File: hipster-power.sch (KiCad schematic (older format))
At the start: 14 parts, among them Q201 FDN340P, SW201 ON|OFF, U201 MCP73831, U202 NCP5501

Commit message: Rename power switch SK12D07VG5 -> SK12D07VG3
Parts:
- SW201: footprint libs:SK12D07VG5 -> libs:SK12D07VG3
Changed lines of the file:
@@
 F 0 "SW201" H 2850 4450 50  0000 C CNN
 F 1 "ON|OFF" H 2850 4250 50  0000 C CNN
-F 2 "libs:SK12D07VG5" H 2850 4350 50  0001 C CNN
+F 2 "libs:SK12D07VG3" H 2850 4350 50  0001 C CNN
 F 3 "" H 2850 4350 50  0000 C CNN
 F 4 "http://www.szlcsc.com/product/details_39247.html" H 7350 2250 60  0001 C CNN "LCSC"

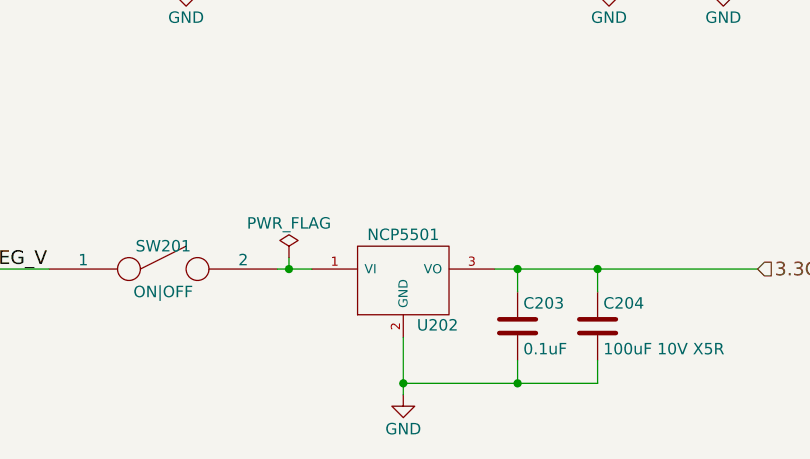
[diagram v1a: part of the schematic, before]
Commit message: Change 3.3V reg to XC6210, enlarge board to move power switch
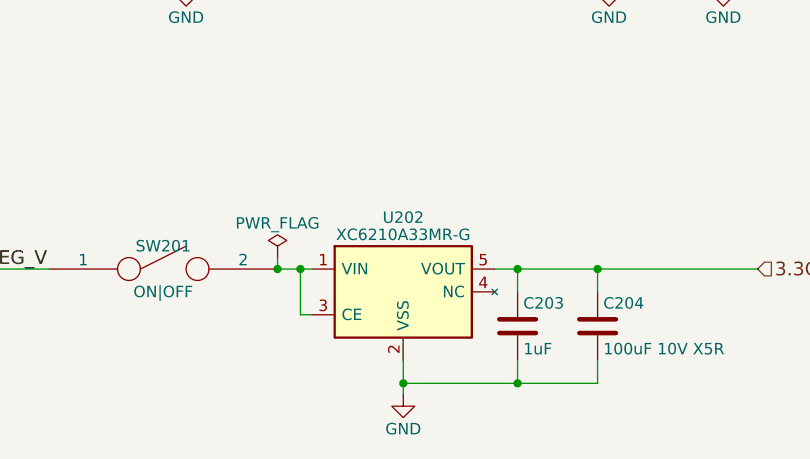
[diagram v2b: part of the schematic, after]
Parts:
- removed U202: NCP5501, libs:DPAK3.NCP5501, symbol NCP5501
- added U202: XC6210A33MR-G, symbol XC6210xxxxMR-G
- C203: value 0.1uF -> 1uF
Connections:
- net 3.3OUT: now also U202.5 (VOUT)
- net at SW201.2: now also U202.1 (VIN), U202.3 (CE)
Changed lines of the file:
@@
 LIBS:valves
 LIBS:ESP32-footprints-Shem-Lib
-LIBS:cp2102
-LIBS:NCP5501
-LIBS:mcp73831
-LIBS:q_pmos_gds
+LIBS:minimum-viable-badge-parts
 LIBS:minimum-viable-badge-cache
 EELAYER 25 0
@@
 UNREG_V
 $Comp
-L NCP5501 U202
-U 1 1 59286CBF
-P 3900 4400
-F 0 "U202" H 4050 4204 50  0000 C CNN
-F 1 "NCP5501" H 3900 4600 50  0000 C CNN
-F 2 "libs:DPAK3.NCP5501" H 3900 4400 50  0001 C CNN
-F 3 "" H 3900 4400 50  0000 C CNN
-F 4 "NCP5501DT33RKGOSCT-ND" H 3900 4400 60  0001 C CNN "Digikey PN"
-F 5 "http://www.digikey.com.au/product-detail/en/on-semiconductor/NCP5501DT33RKG/NCP5501DT33RKGOSCT-ND/3462404" H 3900 4400 60  0001 C CNN "Link"
-F 6 "NCP5501DT33RKG" H 3900 4400 60  0001 C CNN "Manufacture PN"
-F 7 "0.67" H 3900 4400 60  0001 C CNN "Unit Cost"
-	1    3900 4400
-	1    0    0    -1
-$EndComp
-$Comp
 L C C203
 U 1 1 59287000
 P 4400 4600
 F 0 "C203" H 4425 4700 50  0000 L CNN
-F 1 "0.1uF" H 4425 4500 50  0000 L CNN
+F 1 "1uF" H 4425 4500 50  0000 L CNN
 F 2 "Capacitors_SMD:C_0603_HandSoldering" H 4438 4450 50  0001 C CNN
 F 3 "" H 4400 4600 50  0000 C CNN
@@
 L PWR_FLAG #FLG025
 U 1 1 59A7D662
-P 3400 4300
-F 0 "#FLG025" H 3400 4375 50  0001 C CNN
-F 1 "PWR_FLAG" H 3400 4450 50  0000 C CNN
-F 2 "" H 3400 4300 50  0001 C CNN
-F 3 "" H 3400 4300 50  0001 C CNN
-	1    3400 4300
-	1    0    0    -1
-$EndComp
-Wire Wire Line
-	3400 4300 3400 4350
-Connection ~ 3400 4350
+P 3350 4300
+F 0 "#FLG025" H 3350 4375 50  0001 C CNN
+F 1 "PWR_FLAG" H 3350 4450 50  0000 C CNN
+F 2 "" H 3350 4300 50  0001 C CNN
+F 3 "" H 3350 4300 50  0001 C CNN
+	1    3350 4300
+	1    0    0    -1
+$EndComp
+Wire Wire Line
+	3350 4300 3350 4350
+Connection ~ 3350 4350
 $Comp
 L PWR_FLAG #FLG026
@@
 	0    -1   -1   0
 $EndComp
+$Comp
+L XC6210xxxxMR-G U202
+U 1 1 59B66BDA
+P 3900 4450
+F 0 "U202" H 3900 4775 50  0000 C CNN
+F 1 "XC6210A33MR-G" H 3900 4700 50  0000 C CNN
+F 2 "" H 3950 4200 50  0001 L CNN
+F 3 "" H 3900 4450 50  0001 C CNN
+	1    3900 4450
+	1    0    0    -1
+$EndComp
+Wire Wire Line
+	3500 4550 3450 4550
+Wire Wire Line
+	3450 4550 3450 4350
+Connection ~ 3450 4350
 $EndSCHEMATC

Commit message: Fixed some connections.  added vias
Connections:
- net GND: now also U202.2 (VSS)
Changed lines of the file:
@@
 Connection ~ 4400 4350
 Wire Wire Line
-	3900 4650 3900 4900
+	3900 4750 3900 4900
 Wire Wire Line
 	4400 4850 4400 4750

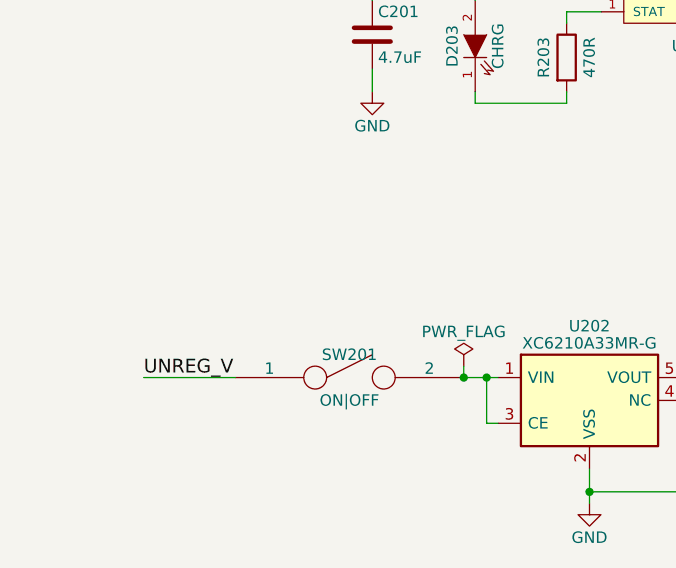
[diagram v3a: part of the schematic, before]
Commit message: Add WS2812Bs for Blinkenlights
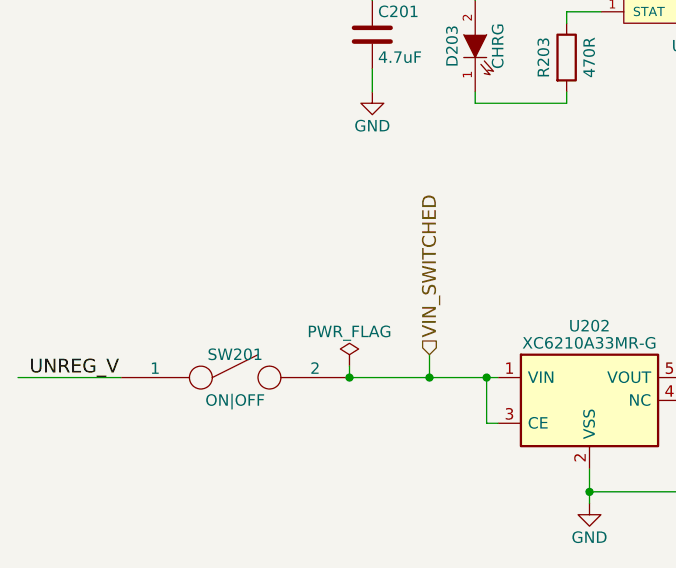
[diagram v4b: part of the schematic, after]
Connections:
- net VIN_SWITCHED: now reaches SW201.2, U202.1 (VIN), U202.3 (CE)
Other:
- moved on the sheet: SW201
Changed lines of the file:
@@
 $Descr A4 11693 8268
 encoding utf-8
-Sheet 2 3
+Sheet 2 4
 Title ""
 Date ""
@@
 L SPST SW201
 U 1 1 59286658
-P 2850 4350
-F 0 "SW201" H 2850 4450 50  0000 C CNN
-F 1 "ON|OFF" H 2850 4250 50  0000 C CNN
-F 2 "libs:SK12D07VG3" H 2850 4350 50  0001 C CNN
-F 3 "" H 2850 4350 50  0000 C CNN
-F 4 "http://www.szlcsc.com/product/details_39247.html" H 7350 2250 60  0001 C CNN "LCSC"
-	1    2850 4350
-	1    0    0    -1
-$EndComp
-Text Label 1950 4350 0    60   ~ 0
+P 2350 4350
+F 0 "SW201" H 2350 4450 50  0000 C CNN
+F 1 "ON|OFF" H 2350 4250 50  0000 C CNN
+F 2 "libs:SK12D07VG3" H 2350 4350 50  0001 C CNN
+F 3 "" H 2350 4350 50  0000 C CNN
+F 4 "http://www.szlcsc.com/product/details_39247.html" H 6850 2250 60  0001 C CNN "LCSC"
+	1    2350 4350
+	1    0    0    -1
+$EndComp
+Text Label 1450 4350 0    60   ~ 0
 UNREG_V
 $Comp
@@
 Connection ~ 2950 2550
 Wire Wire Line
-	1950 4350 2350 4350
-Wire Wire Line
-	3350 4350 3500 4350
+	2850 4350 3500 4350
 Wire Wire Line
 	4300 4350 5450 4350
@@
 L PWR_FLAG #FLG025
 U 1 1 59A7D662
-P 3350 4300
-F 0 "#FLG025" H 3350 4375 50  0001 C CNN
-F 1 "PWR_FLAG" H 3350 4450 50  0000 C CNN
-F 2 "" H 3350 4300 50  0001 C CNN
-F 3 "" H 3350 4300 50  0001 C CNN
-	1    3350 4300
-	1    0    0    -1
-$EndComp
-Wire Wire Line
-	3350 4300 3350 4350
-Connection ~ 3350 4350
+P 2850 4300
+F 0 "#FLG025" H 2850 4375 50  0001 C CNN
+F 1 "PWR_FLAG" H 2850 4450 50  0000 C CNN
+F 2 "" H 2850 4300 50  0001 C CNN
+F 3 "" H 2850 4300 50  0001 C CNN
+	1    2850 4300
+	1    0    0    -1
+$EndComp
+Wire Wire Line
+	2850 4300 2850 4350
+Connection ~ 2850 4350
 $Comp
 L PWR_FLAG #FLG026
@@
 	3450 4550 3450 4350
 Connection ~ 3450 4350
+Text HLabel 3200 4250 1    60   Input ~ 0
+VIN_SWITCHED
+Wire Wire Line
+	1850 4350 1400 4350
+Wire Wire Line
+	3200 4250 3200 4350
+Connection ~ 3200 4350
 $EndSCHEMATC

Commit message: Route LEDs, make edge connector one sided with mounting slots
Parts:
- U202: footprint (none) -> TO_SOT_Packages_SMD:SOT-23-5_HandSoldering
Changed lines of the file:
@@
 F 0 "U202" H 3900 4775 50  0000 C CNN
 F 1 "XC6210A33MR-G" H 3900 4700 50  0000 C CNN
-F 2 "" H 3950 4200 50  0001 L CNN
+F 2 "TO_SOT_Packages_SMD:SOT-23-5_HandSoldering" H 3950 4200 50  0001 L CNN
 F 3 "" H 3900 4450 50  0001 C CNN
 	1    3900 4450
